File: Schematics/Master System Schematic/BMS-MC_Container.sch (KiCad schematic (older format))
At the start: 8 parts, among them K1 Cooling Pump Shutoff Relay, K53 BMS_PWR_Relay, K54 Cooling Pump Relay, U3 RinehartPM100DX_MotorControll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, U6 OrionBMS2, U7 OrionThermExp

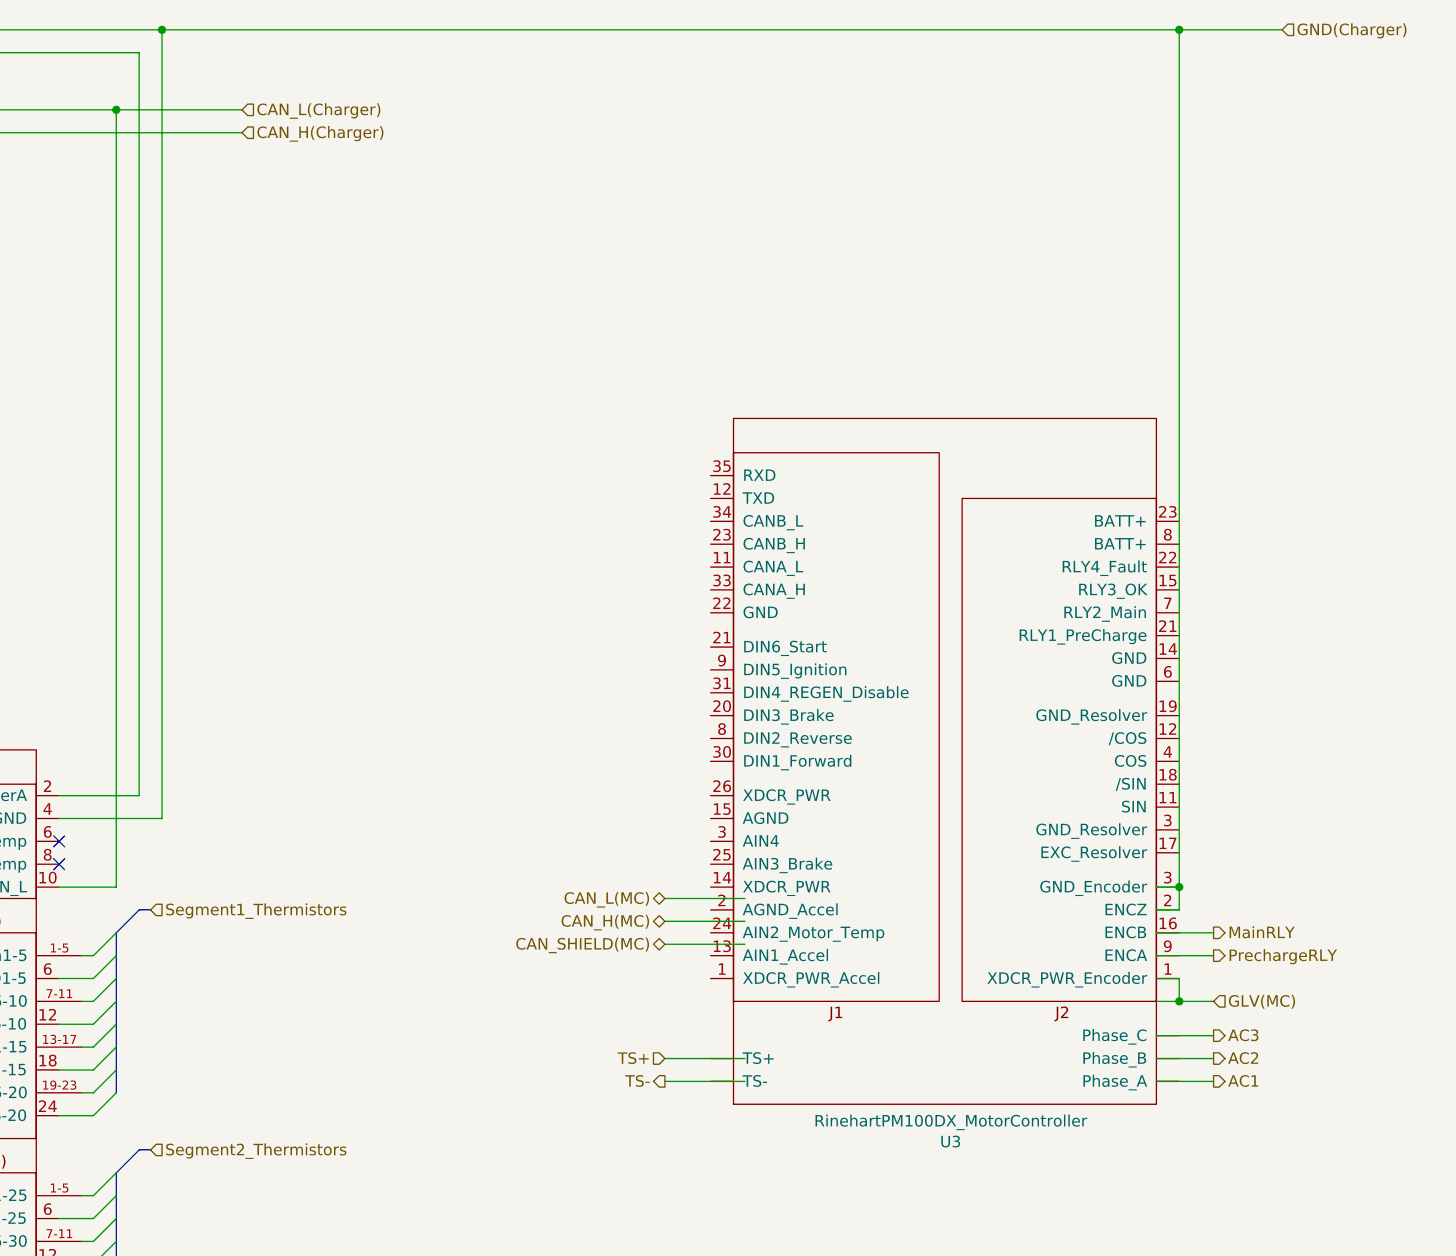
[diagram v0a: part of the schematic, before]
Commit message: MC Part Update
Updated MC and motor schematic parts
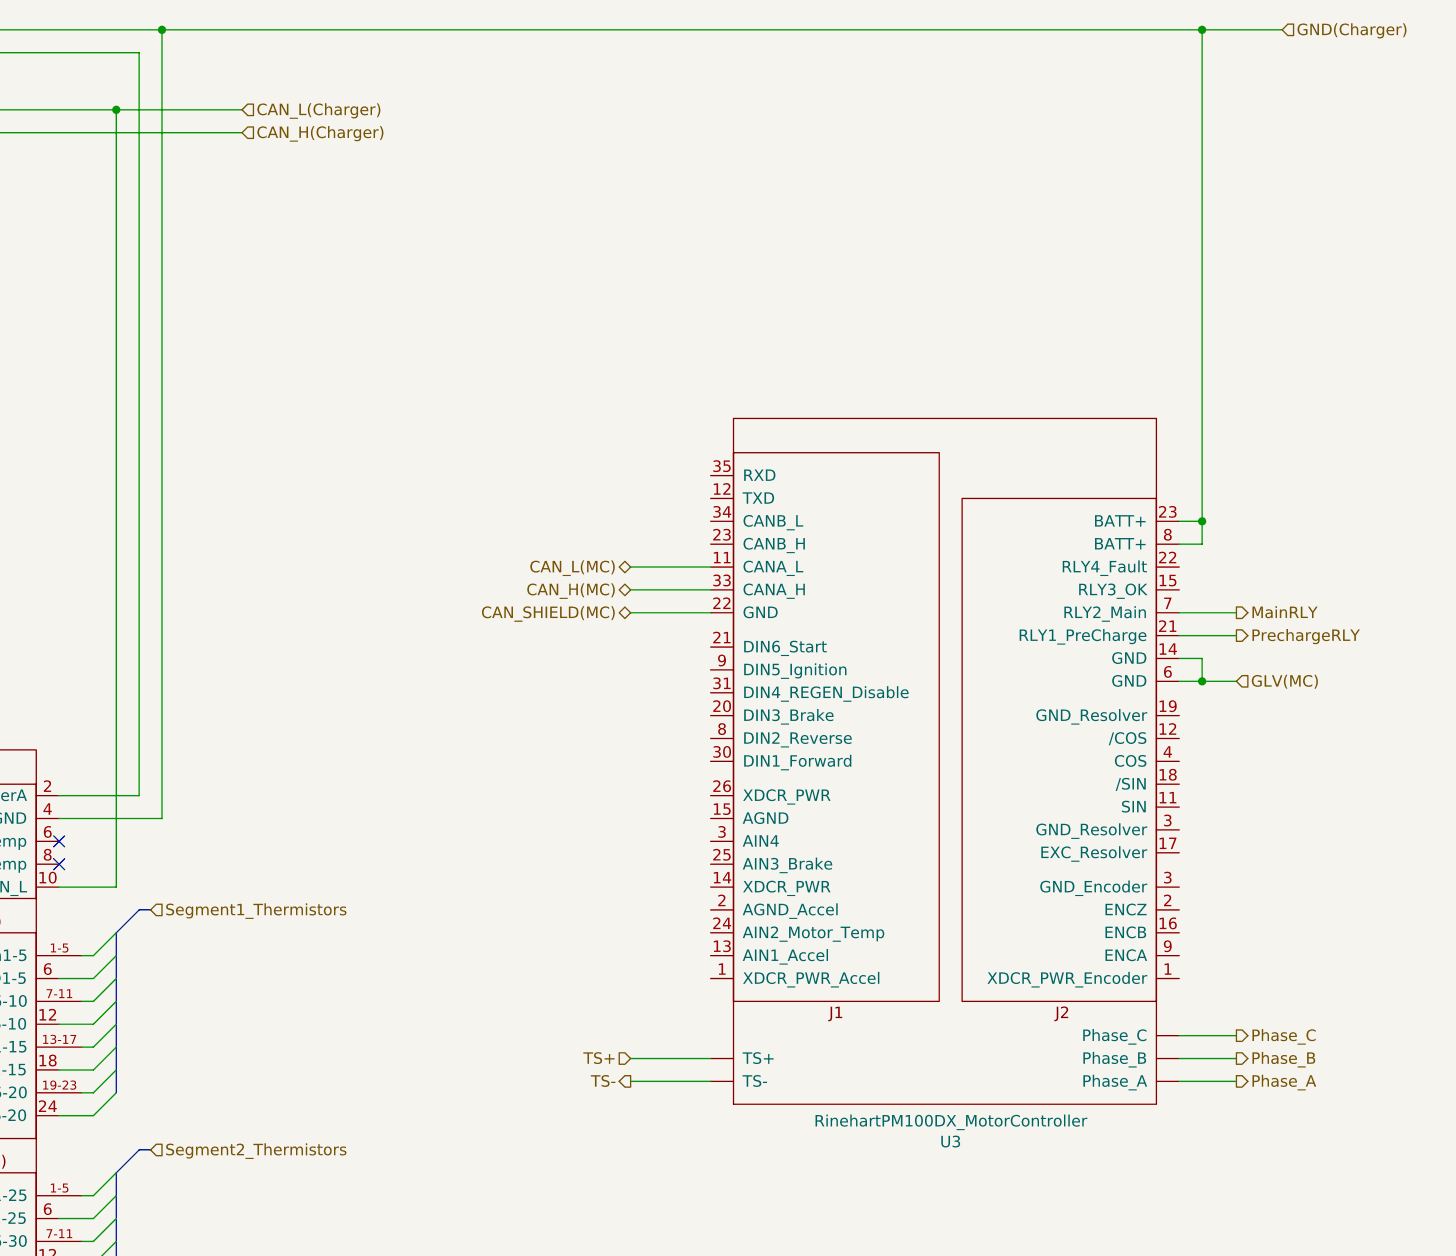
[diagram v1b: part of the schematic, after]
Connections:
- net labels added: Phase_A, Phase_B, Phase_C
- net labels removed: AC1, AC2, AC3
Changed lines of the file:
@@
 Wire Wire Line
 	4800 3300 5900 3300
-$Comp
-L NER:RinehartPM100DX_MotorController U?
-U 1 1 62DE1334
-P 14000 5950
-AR Path="/62DE1334" Ref="U?"  Part="1"
-AR Path="/60D53BFB/62DE1334" Ref="U3"  Part="1"
-F 0 "U3" H 14000 6115 50  0000 C CNN
-F 1 "RinehartPM100DX_MotorController" H 14000 6024 50  0000 C CNN
-F 2 "" H 14000 5950 50  0001 C CNN
-F 3 "" H 14000 5950 50  0001 C CNN
-	1    14000 5950
-	1    0    0    1
-$EndComp
-Text HLabel 12750 5750 0    50   Input ~ 0
+Text HLabel 12600 5750 0    50   Input ~ 0
 TS+
-Text HLabel 12750 5850 0    50   Output ~ 0
+Text HLabel 12600 5850 0    50   Output ~ 0
 TS-
 Wire Wire Line
-	12750 5750 13100 5750
+	12600 5750 12950 5750
 Wire Wire Line
-	13100 5850 12750 5850
+	12950 5850 12600 5850
 Wire Wire Line
-	13100 5150 12750 5150
+	12950 3700 12600 3700
 Wire Wire Line
-	13100 5050 12750 5050
+	12950 3600 12600 3600
 Wire Wire Line
-	13100 5250 12750 5250
-Wire Wire Line
-	14900 5300 15150 5300
-Wire Wire Line
-	14900 5500 15000 5500
-Wire Wire Line
-	14900 5400 15000 5400
-Wire Wire Line
-	15000 5400 15000 5500
-Connection ~ 15000 5500
-Wire Wire Line
-	15000 5500 15150 5500
-Text HLabel 12750 5050 0    50   BiDi ~ 0
+	12950 3800 12600 3800
+Text HLabel 12600 3600 0    50   BiDi ~ 0
 CAN_L(MC)
-Text HLabel 12750 5150 0    50   BiDi ~ 0
+Text HLabel 12600 3700 0    50   BiDi ~ 0
 CAN_H(MC)
-Text HLabel 12750 5250 0    50   BiDi ~ 0
+Text HLabel 12600 3800 0    50   BiDi ~ 0
 CAN_SHIELD(MC)
-Text HLabel 15150 5300 2    50   Output ~ 0
+Text HLabel 15250 3900 2    50   Output ~ 0
 PrechargeRLY
-Text HLabel 15150 5500 2    50   Input ~ 0
-GLV(MC)
-Text HLabel 15150 5650 2    50   Output ~ 0
-AC3
-Text HLabel 15150 5750 2    50   Output ~ 0
-AC2
-Text HLabel 15150 5850 2    50   Output ~ 0
-AC1
-Wire Wire Line
-	14900 5650 15150 5650
-Wire Wire Line
-	15150 5750 14900 5750
-Wire Wire Line
-	14900 5850 15150 5850
-Text HLabel 15150 5200 2    50   Output ~ 0
+Text HLabel 15250 5650 2    50   Output ~ 0
+Phase_C
+Text HLabel 15250 5750 2    50   Output ~ 0
+Phase_B
+Text HLabel 15250 5850 2    50   Output ~ 0
+Phase_A
+Text HLabel 15250 3800 2    50   Output ~ 0
 MainRLY
 Wire Wire Line
@@
 Connection ~ 3350 3800
 Wire Wire Line
-	10550 1250 15000 1250
+	10550 1250 15100 1250
 Wire Wire Line
-	14900 5100 15000 5100
+	15000 5850 15250 5850
+Text HLabel 15250 4100 2    50   Input ~ 0
+GLV(MC)
 Wire Wire Line
-	15000 5100 15000 5000
-Connection ~ 15000 1250
+	15250 5750 15000 5750
 Wire Wire Line
-	15000 1250 15450 1250
+	15000 5650 15250 5650
 Wire Wire Line
-	14900 5000 15000 5000
-Connection ~ 15000 5000
+	15000 3900 15250 3900
 Wire Wire Line
-	15000 5000 15000 1250
+	15000 3800 15250 3800
+$Comp
+L NER:RinehartPM100DX_MotorController U?
+U 1 1 62DE1334
+P 14000 5950
+AR Path="/62DE1334" Ref="U?"  Part="1"
+AR Path="/60D53BFB/62DE1334" Ref="U3"  Part="1"
+F 0 "U3" H 14000 6115 50  0000 C CNN
+F 1 "RinehartPM100DX_MotorController" H 14000 6024 50  0000 C CNN
+F 2 "" H 14000 5950 50  0001 C CNN
+F 3 "" H 14000 5950 50  0001 C CNN
+	1    14000 5950
+	1    0    0    1
+$EndComp
 Wire Wire Line
-	14900 5200 15150 5200
+	15000 4100 15100 4100
+Wire Wire Line
+	15000 4000 15100 4000
+Wire Wire Line
+	15100 4000 15100 4100
+Connection ~ 15100 4100
+Wire Wire Line
+	15100 4100 15250 4100
+Wire Wire Line
+	15000 3500 15100 3500
+Wire Wire Line
+	15100 3500 15100 3400
+Connection ~ 15100 1250
+Wire Wire Line
+	15100 1250 15450 1250
+Wire Wire Line
+	15000 3400 15100 3400
 Wire Bus Line
 	5650 8200 5650 8500
@@
 Wire Bus Line
 	10350 6250 10350 6950
+Connection ~ 15100 3400
+Wire Wire Line
+	15100 3400 15100 1250
 $EndSCHEMATC

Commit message: Moved Thermistor Exp and MC out of BMS container
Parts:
- removed U3: RinehartPM100DX_MotorController, symbol NER:RinehartPM100DX_MotorController
- removed U7: OrionThermExp, symbol NER:OrionThermExp
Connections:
- net GLV(BMS+Charging) is gone; now on net GLV(BMS): D32.2 (K), K53.6, U6.2 (RM1-)
- net GLV(BMS): now reaches U6.2 (RM1-)
- net at U6.3 (RM2+): now also K53.7, K53.8
- no-connect marks 29 -> 26

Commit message: Wired MC
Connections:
- net at U6.3 (RM2+): now also K53.7, K53.8
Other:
- moved on the sheet: D31, D32, K1, K53, K54, U6

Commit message: Re-wiring
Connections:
- net at U6.3 (RM2+): now also K53.7, K53.8
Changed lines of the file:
@@
 Text HLabel 4850 1650 0    50   Input ~ 0
 GLV(BMS)
-Text HLabel 4850 1550 0    50   Output ~ 0
+Text HLabel 4850 1550 0    50   UnSpc ~ 0
 GND
 Text HLabel 6300 7450 0    50   Input ~ 0
@@
 Wire Wire Line
 	6250 7200 6700 7200
-Text HLabel 4800 2800 0    50   Output ~ 0
+Text HLabel 4800 2800 0    50   Input ~ 0
 ChargerPWR
 $Comp
@@
 Wire Wire Line
 	8950 2800 9850 2800
-Text HLabel 7850 3600 0    50   Input ~ 0
+Text HLabel 4800 3600 0    50   Input ~ 0
 CoolingPumpPower_IN
-Text HLabel 9900 3600 2    50   Input ~ 0
+Text HLabel 9900 3600 2    50   Output ~ 0
 CoolingPumpPower_OUT
 Wire Wire Line
@@
 Wire Wire Line
 	9850 3200 9850 2800
-Text HLabel 7850 3200 0    50   Input ~ 0
+Text HLabel 4800 3200 0    50   Input ~ 0
 CoolingPumpControl
-Wire Wire Line
-	7850 3200 8350 3200
 Text HLabel 14100 2000 2    50   Input ~ 0
 CAN_H(Charger)
@@
 $EndComp
 Wire Wire Line
-	7850 3600 8000 3600
-Wire Wire Line
 	8000 2850 8000 2800
 Connection ~ 8000 2800
@@
 Wire Wire Line
 	9850 1550 14100 1550
+Wire Wire Line
+	4800 3200 8350 3200
+Wire Wire Line
+	4800 3600 8000 3600
 Wire Bus Line
 	8850 8500 8850 8800

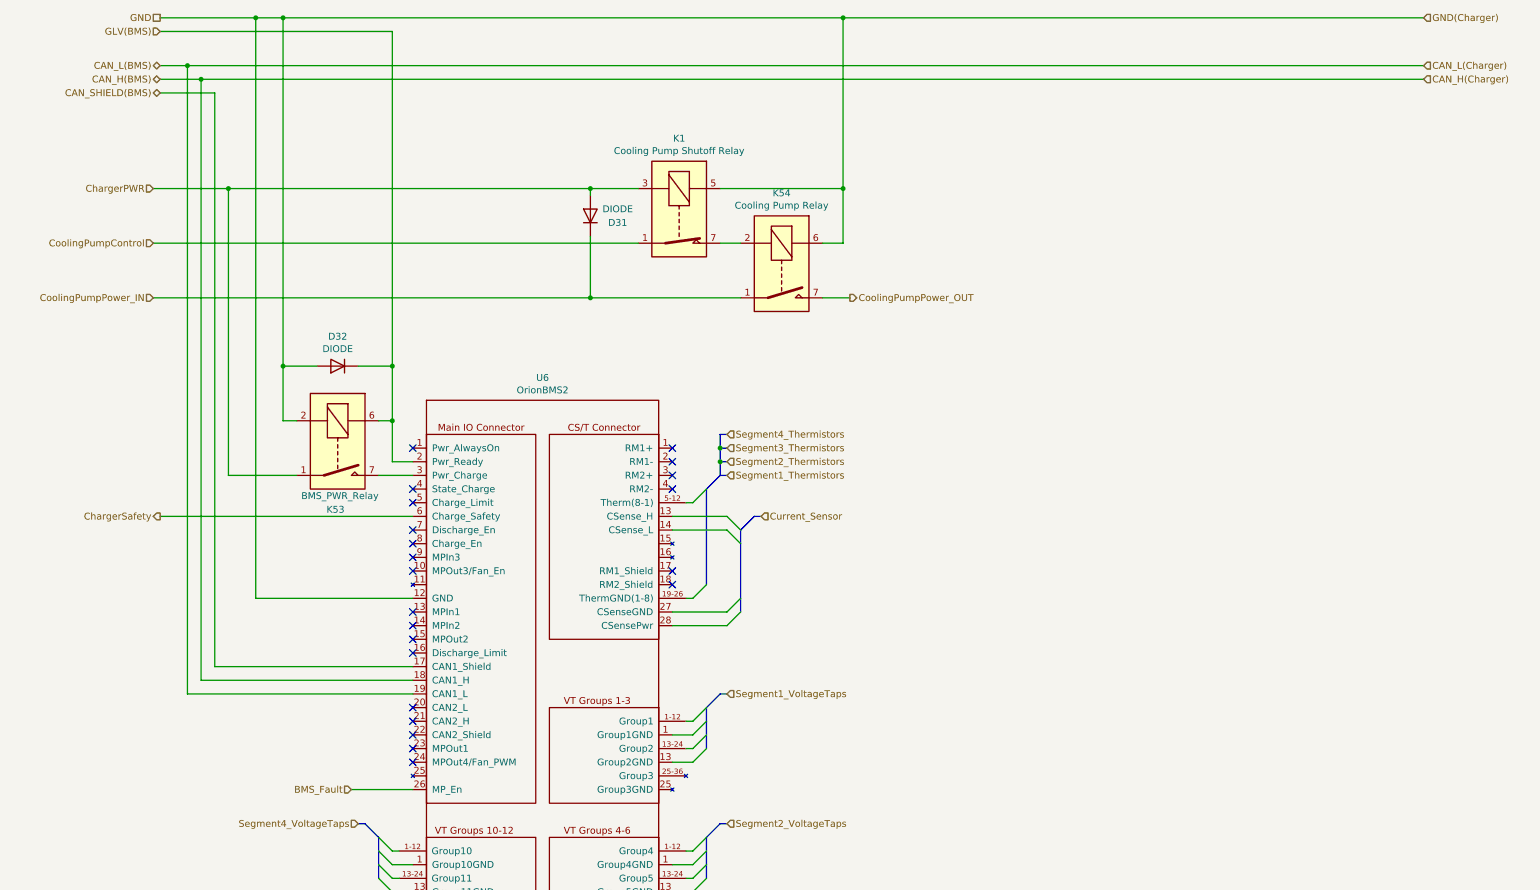
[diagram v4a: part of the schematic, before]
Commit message: Wiring Cleanup and sheet pin fixing
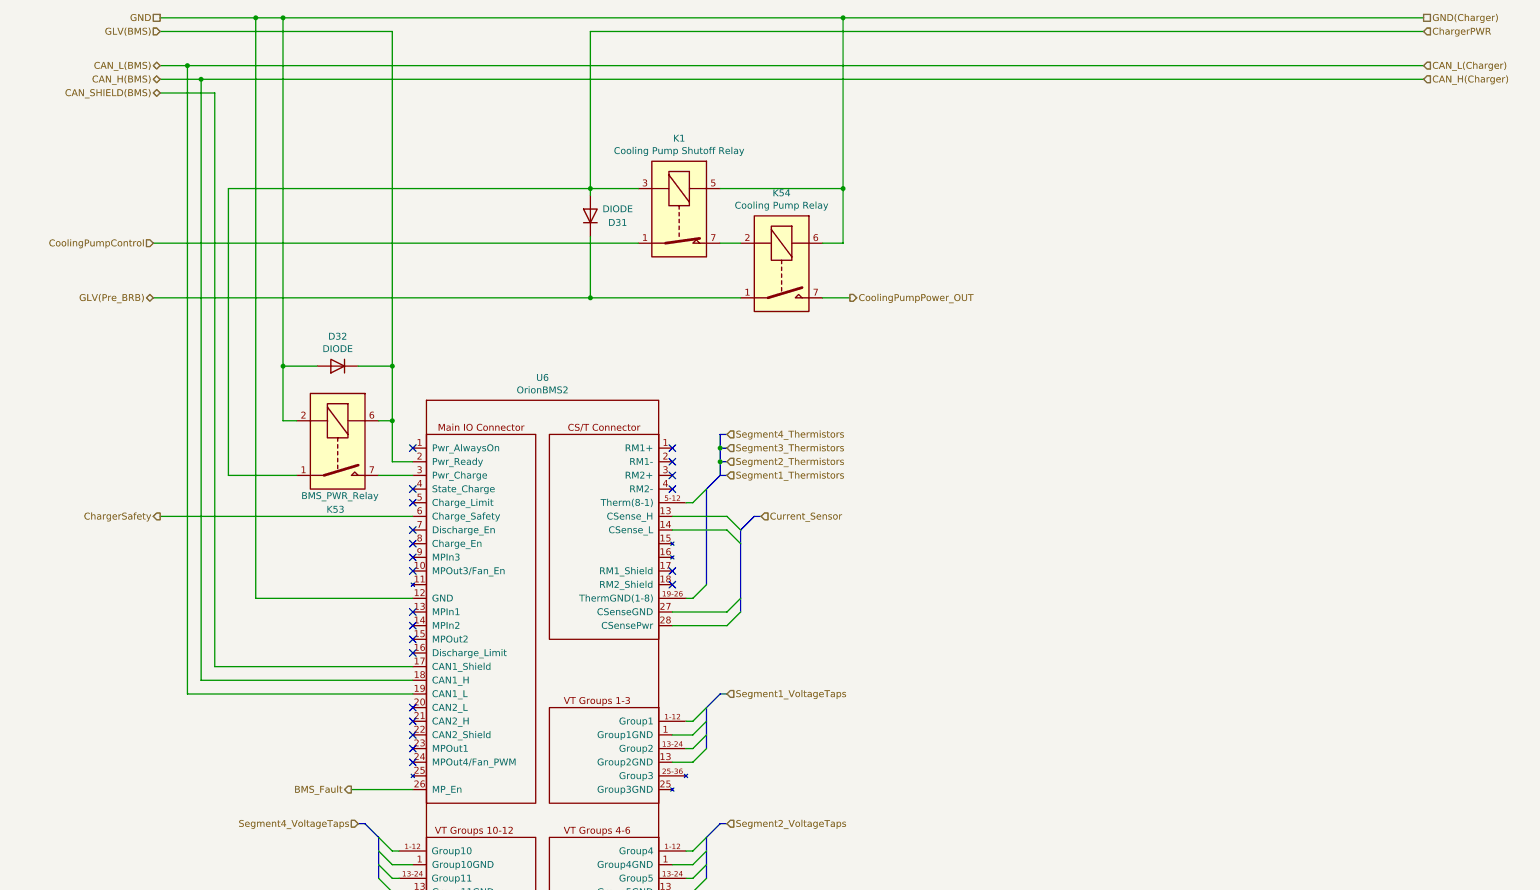
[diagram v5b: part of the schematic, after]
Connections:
- net at U6.3 (RM2+): now also K53.7, K53.8
- net CoolingPumpPower_IN renamed GLV(Pre_BRB)
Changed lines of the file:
@@
 Sheet 21 22
 Title "BMS & MC Container"
-Date "2020-11-03"
-Rev "5"
+Date "2020-11-11"
+Rev "6"
 Comp "Northeastern Electric Racing"
 Comment1 "https://github.com/Northeastern-Electric-Racing/NER"
@@
 Text HLabel 6300 7450 0    50   Input ~ 0
 Segment4_VoltageTaps
-Text HLabel 6250 7200 0    50   Input ~ 0
+Text HLabel 6250 7200 0    50   Output ~ 0
 BMS_Fault
 Text HLabel 9250 5200 2    50   Input ~ 0
@@
 Wire Wire Line
 	6250 7200 6700 7200
-Text HLabel 4800 2800 0    50   Input ~ 0
+Text HLabel 14100 1650 2    50   Input ~ 0
 ChargerPWR
 $Comp
@@
 Wire Wire Line
 	8950 2800 9850 2800
-Text HLabel 4800 3600 0    50   Input ~ 0
-CoolingPumpPower_IN
+Text HLabel 4800 3600 0    50   BiDi ~ 0
+GLV(Pre_BRB)
 Text HLabel 9900 3600 2    50   Output ~ 0
 CoolingPumpPower_OUT
@@
 Text HLabel 14100 1900 2    50   Input ~ 0
 CAN_L(Charger)
-Text HLabel 14100 1550 2    50   Input ~ 0
+Text HLabel 14100 1550 2    50   UnSpc ~ 0
 GND(Charger)
 $Comp
@@
 Connection ~ 9850 1550
 Wire Wire Line
-	4800 2800 5350 2800
-Wire Wire Line
 	5350 2800 5350 4900
-Connection ~ 5350 2800
 Wire Wire Line
 	5350 2800 8000 2800
@@
 Wire Wire Line
 	4800 3600 8000 3600
+Wire Wire Line
+	8000 1650 8000 2800
+Wire Wire Line
+	8000 1650 14100 1650
 Wire Bus Line
 	8850 8500 8850 8800
